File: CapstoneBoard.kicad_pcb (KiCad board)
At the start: 2 copper layers, 92.5 x 59.6 mm, 42 parts, among them J1 Battery Conn, J10 Conn_02x02_Odd_Even, J2 IMU_COMM, J3 IMU_EXTRA, J4 SERVO_FEEDBACK, J5 Conn_FLIR, J6 Conn_LIDAR, J7 Conn_Servo_Driver, J8 Conn_01x04, J9 Jetson_Nano_Header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

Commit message: PCB Rev 3
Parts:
- removed J10: Conn_02x02_Odd_Even, Connector_PinHeader_2.54mm:PinHeader_2x02_P2.54mm_Vertical
- added C11: 100n, Capacitor_SMD:C_1206_3216Metric_Pad1.33x1.80mm_HandSolder, F.Cu at (162.2, 90.8)
- added J11: Conn_01x04, Connector_PinHeader_2.54mm:PinHeader_1x06_P2.54mm_Vertical, F.Cu at (170.0, 60.9)
- added J12: Conn_01x02, Connector_PinHeader_2.54mm:PinHeader_1x02_P2.54mm_Vertical, F.Cu at (146.7, 74.2)
- added JP1: WP, Jumper:SolderJumper-2_P1.3mm_Open_Pad1.0x1.5mm, F.Cu at (158.2, 81.6)
- added R1: 1k, Resistor_SMD:R_1206_3216Metric_Pad1.30x1.75mm_HandSolder, F.Cu at (165.9, 82.4)
- added R12: 3.9k, Resistor_SMD:R_1206_3216Metric_Pad1.30x1.75mm_HandSolder, F.Cu at (162.4, 78.2)
- added R13: 3.9k, Resistor_SMD:R_1206_3216Metric_Pad1.30x1.75mm_HandSolder, F.Cu at (162.8, 75.5)
- added U3: CAT24C32, Package_SO:TSSOP-8_4.4x3mm_P0.65mm, F.Cu at (161.4, 83.9)
- moved H6 2.03 mm to (85.0, 58.0)
- moved H5 1.47 mm to (85.0, 103.0)
- moved R3 1.45 mm to (111.7, 89.2)
- moved H1 0.42 mm to (169.0, 66.0)
- moved H3 0.42 mm to (169.0, 87.6)
- moved J2 0.42 mm to (170.3, 83.1)
- moved J3 0.42 mm to (152.5, 80.6)
- moved H2 0.42 mm to (153.8, 87.6)
- moved H4 0.42 mm to (153.8, 66.0)
- moved H7 0.22 mm to (169.0, 103.3)
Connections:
- J9 pad 12: (no net) -> /I2S_SCK
- J9 pad 27: /SDA2 -> /ID_SD
- J9 pad 28: /SCL2 -> /ID_SC
- J9 pad 31: (no net) -> /GPIO6
- J9 pad 32: (no net) -> /GPIO12
- J9 pad 35: (no net) -> /I2S_FS
- J9 pad 38: (no net) -> /I2S_DIN
- J9 pad 40: (no net) -> /I2S_DOUT
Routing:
- net /I2S_SCK: track 0.00 -> 37.5 mm
- net +BATT: track 89.4 -> 122.7 mm, vias 1 -> 0
- net /ID_SC: track 0.00 -> 28.5 mm, vias 0 -> 1
- net /ID_SD: track 0.00 -> 26.2 mm, vias 0 -> 1
- net +3V3: track 132.3 -> 156.7 mm
- net /WP: track 0.00 -> 11.1 mm
- net /SCL2: track 10.9 -> 0.00 mm
- net GND: track 6.84 -> 16.4 mm
- net /CS_FLIR: track 51.0 -> 60.2 mm
- net /SDA1: track 159.3 -> 151.3 mm
- net /I2S_DOUT: track 0.00 -> 7.32 mm
- net /GPIO12: track 0.00 -> 7.02 mm
- net /I2S_DIN: track 0.00 -> 7.01 mm
- net /SDA2: track 6.96 -> 0.00 mm
- net /MISO1: track 58.6 -> 54.4 mm
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
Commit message: Revision 3 completed
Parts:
- moved J11 0.63 mm to (170.0, 61.6)
- moved R6 0.51 mm to (111.2, 95.0)
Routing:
- net GND: track 16.4 -> 83.6 mm
- net /PSU_SENS: track 70.4 -> 88.5 mm
- net /PSU_SW1: track 15.0 -> 27.3 mm
- net /PSU_VOUT: track 6.63 -> 13.7 mm
- net /I2S_DIN: track 7.01 -> 7.91 mm
- removed copper zone on F.Cu, net /PSU_SW1
- removed copper zone on F.Cu, net /PSU_VOUT

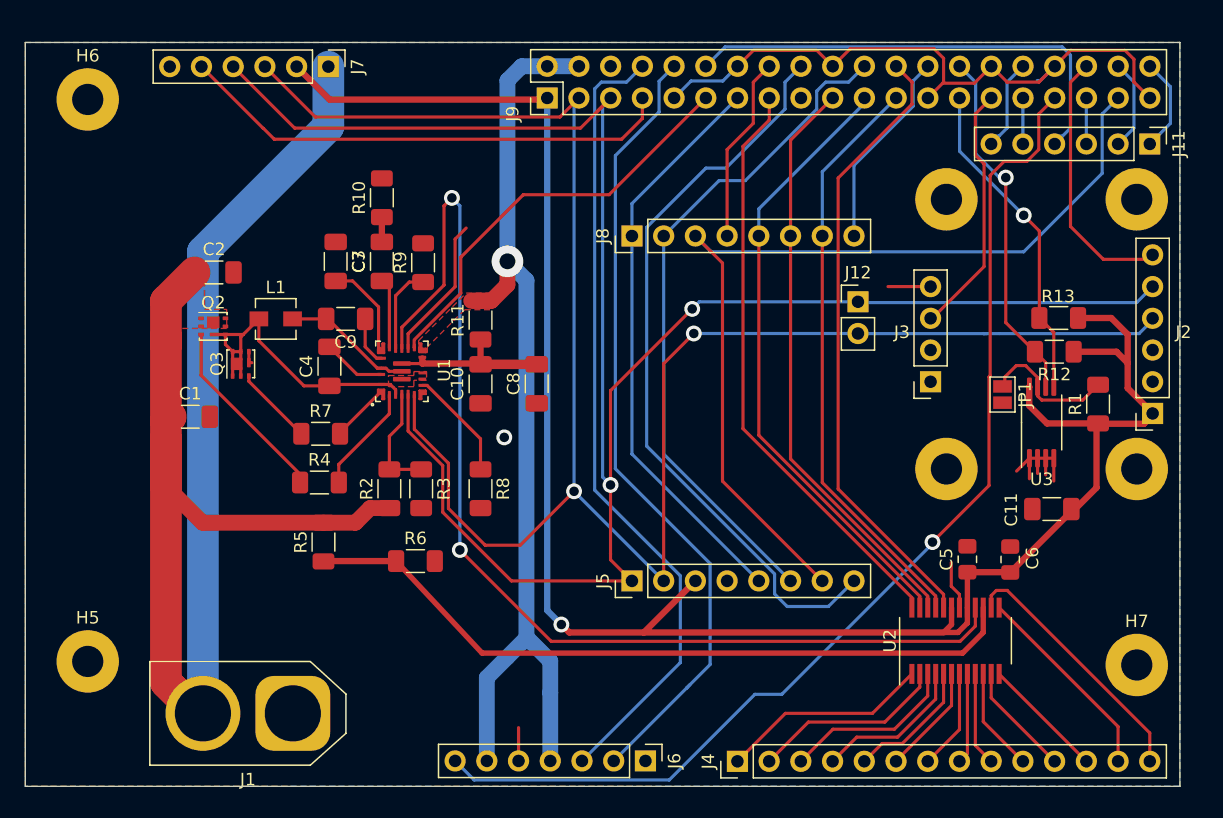
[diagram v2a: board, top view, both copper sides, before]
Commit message: Update board for better soldering without plated drills.
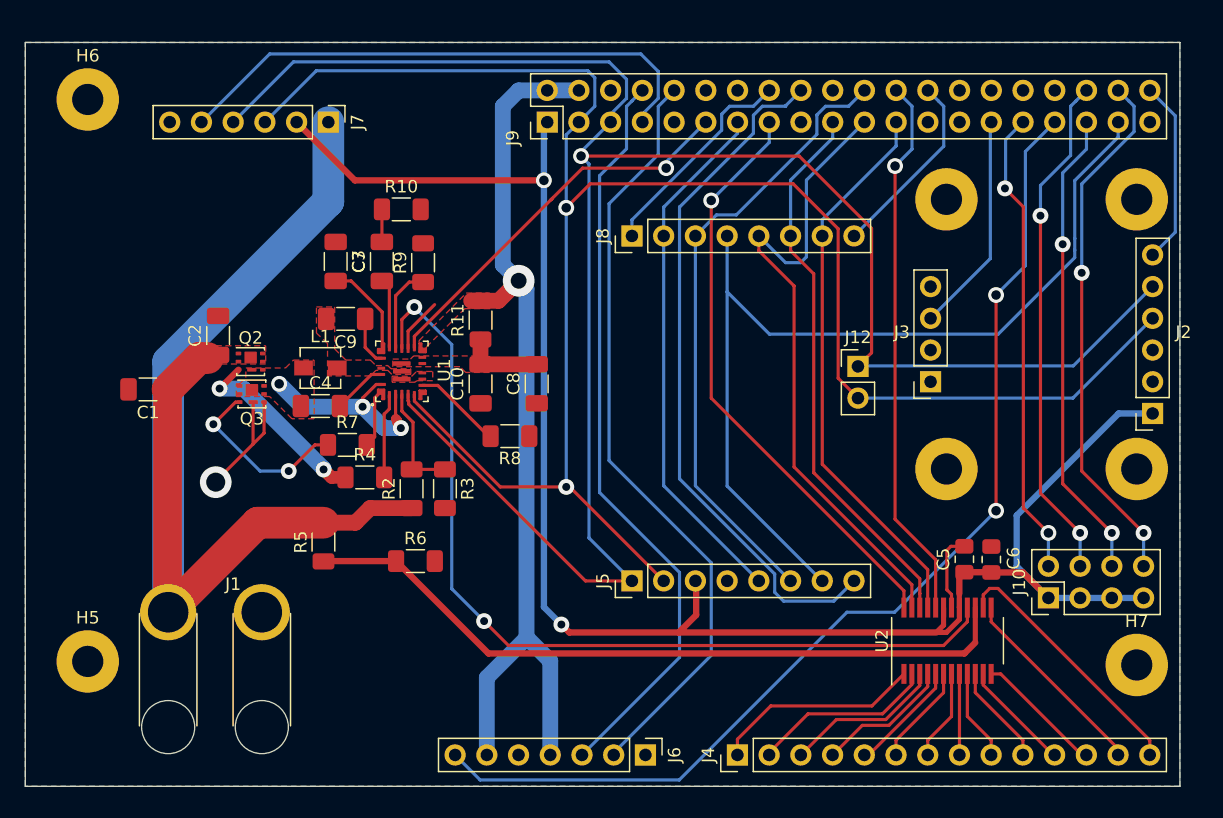
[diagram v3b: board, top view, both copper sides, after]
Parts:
- removed C11: 100n, Capacitor_SMD:C_1206_3216Metric_Pad1.33x1.80mm_HandSolder
- removed J11: Conn_01x04, Connector_PinHeader_2.54mm:PinHeader_1x06_P2.54mm_Vertical
- removed JP1: WP, Jumper:SolderJumper-2_P1.3mm_Open_Pad1.0x1.5mm
- removed R1: 1k, Resistor_SMD:R_1206_3216Metric_Pad1.30x1.75mm_HandSolder
- removed R12, R13: 3.9k, Resistor_SMD:R_1206_3216Metric_Pad1.30x1.75mm_HandSolder
- removed U3: CAT24C32, Package_SO:TSSOP-8_4.4x3mm_P0.65mm
- added J10: CONN_FEET, Connector_PinHeader_2.54mm:PinHeader_2x04_P2.54mm_Vertical, F.Cu at (161.9, 97.9)
- J1: footprint Connector_AMASS:AMASS_XT60-M_1x02_P7.20mm_Vertical -> CapstoneParts:wireConn2
- moved J1 12.9 mm to (91.4, 99.1), turned to 0 degrees
- moved L1 5.32 mm to (103.6, 79.5)
- moved J12 5.17 mm to (146.7, 79.4)
- moved C2 5.06 mm to (95.4, 76.9), turned to 90 degrees
- moved R8 4.82 mm to (118.8, 85.0), turned to 0 degrees
- moved J7 4.45 mm to (104.3, 59.8)
- moved Q2 4.11 mm to (98.0, 79.0)
- moved C1 4.03 mm to (89.8, 81.2), turned to 180 degrees
- moved R4 3.66 mm to (107.2, 88.3)
- moved C4 3.26 mm to (103.6, 82.5), turned to 0 degrees
- moved Q3 2.57 mm to (98.1, 81.6), turned to 0 degrees
- moved R7 2.32 mm to (105.8, 85.7)
- moved J9 1.94 mm to (121.8, 59.8)
- moved R3 1.90 mm to (113.6, 89.2)
- moved R10 1.81 mm to (110.1, 66.8), turned to 0 degrees
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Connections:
- J1 pad 1: GND -> +BATT
- J1 pad 2: +BATT -> GND
- J8 pad 1: /SCLK1 -> /SPI0_CS0
- J8 pad 2: /MISO1 -> /SCLK1
- J8 pad 3: /MOSI1 -> /MISO1
- J8 pad 4: /SPI0_CS0 -> /MOSI1
- J9 pad 12: /I2S_SCK -> (no net)
- J9 pad 17: +3V3 -> (no net)
- J9 pad 27: /ID_SD -> (no net)
- J9 pad 28: /ID_SC -> (no net)
- J9 pad 31: /GPIO6 -> /SW_BL
- J9 pad 32: /GPIO12 -> (no net)
- J9 pad 35: /I2S_FS -> /SW_FL
- J9 pad 36: /IMU_RST -> /SW_BR
- J9 pad 38: /I2S_DIN -> /SW_FR
- J9 pad 40: /I2S_DOUT -> /IMU_RST
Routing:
- net GND: track 83.6 -> 22.0 mm
- net /SW_FR: track 0.00 -> 42.4 mm, vias 0 -> 2
- net /SW_BR: track 0.00 -> 40.9 mm, vias 0 -> 2
- net /SW_FL: track 0.00 -> 38.0 mm, vias 0 -> 2
- net /SW_BL: track 0.00 -> 37.6 mm, vias 0 -> 2
- net /I2S_SCK: track 37.5 -> 0.00 mm
- net +BATT: track 122.8 -> 89.6 mm
- net /ID_SC: track 28.8 -> 0.00 mm, vias 1 -> 0
- net /ID_SD: track 26.2 -> 0.00 mm, vias 1 -> 0
- net /PSU_SENS: track 88.5 -> 72.6 mm
- net +3V3: track 156.7 -> 143.3 mm, vias 1 -> 2
- net /WP: track 11.1 -> 0.00 mm
- net /PSU_SW1: track 27.3 -> 16.8 mm, vias 0 -> 3
- net /PSU_SW2: track 9.89 -> 0.00 mm
- net Net-(Q3-Pad3): track 6.36 -> 14.4 mm, vias 0 -> 2
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- added copper zone on F.Cu, net /PSU_SW1
- added copper zone on F.Cu, net /PSU_SW2
- added copper zone on F.Cu, net /PSU_VOUT
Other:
- net class PS_VOUT_SPECIAL added: clearance 0.2032, trace_width 0.254, via_dia 1.27, via_drill 0.762
